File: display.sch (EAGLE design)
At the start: 69 parts, among them IC1 74595, IC2 74595, IC3 74595, IC4 74595

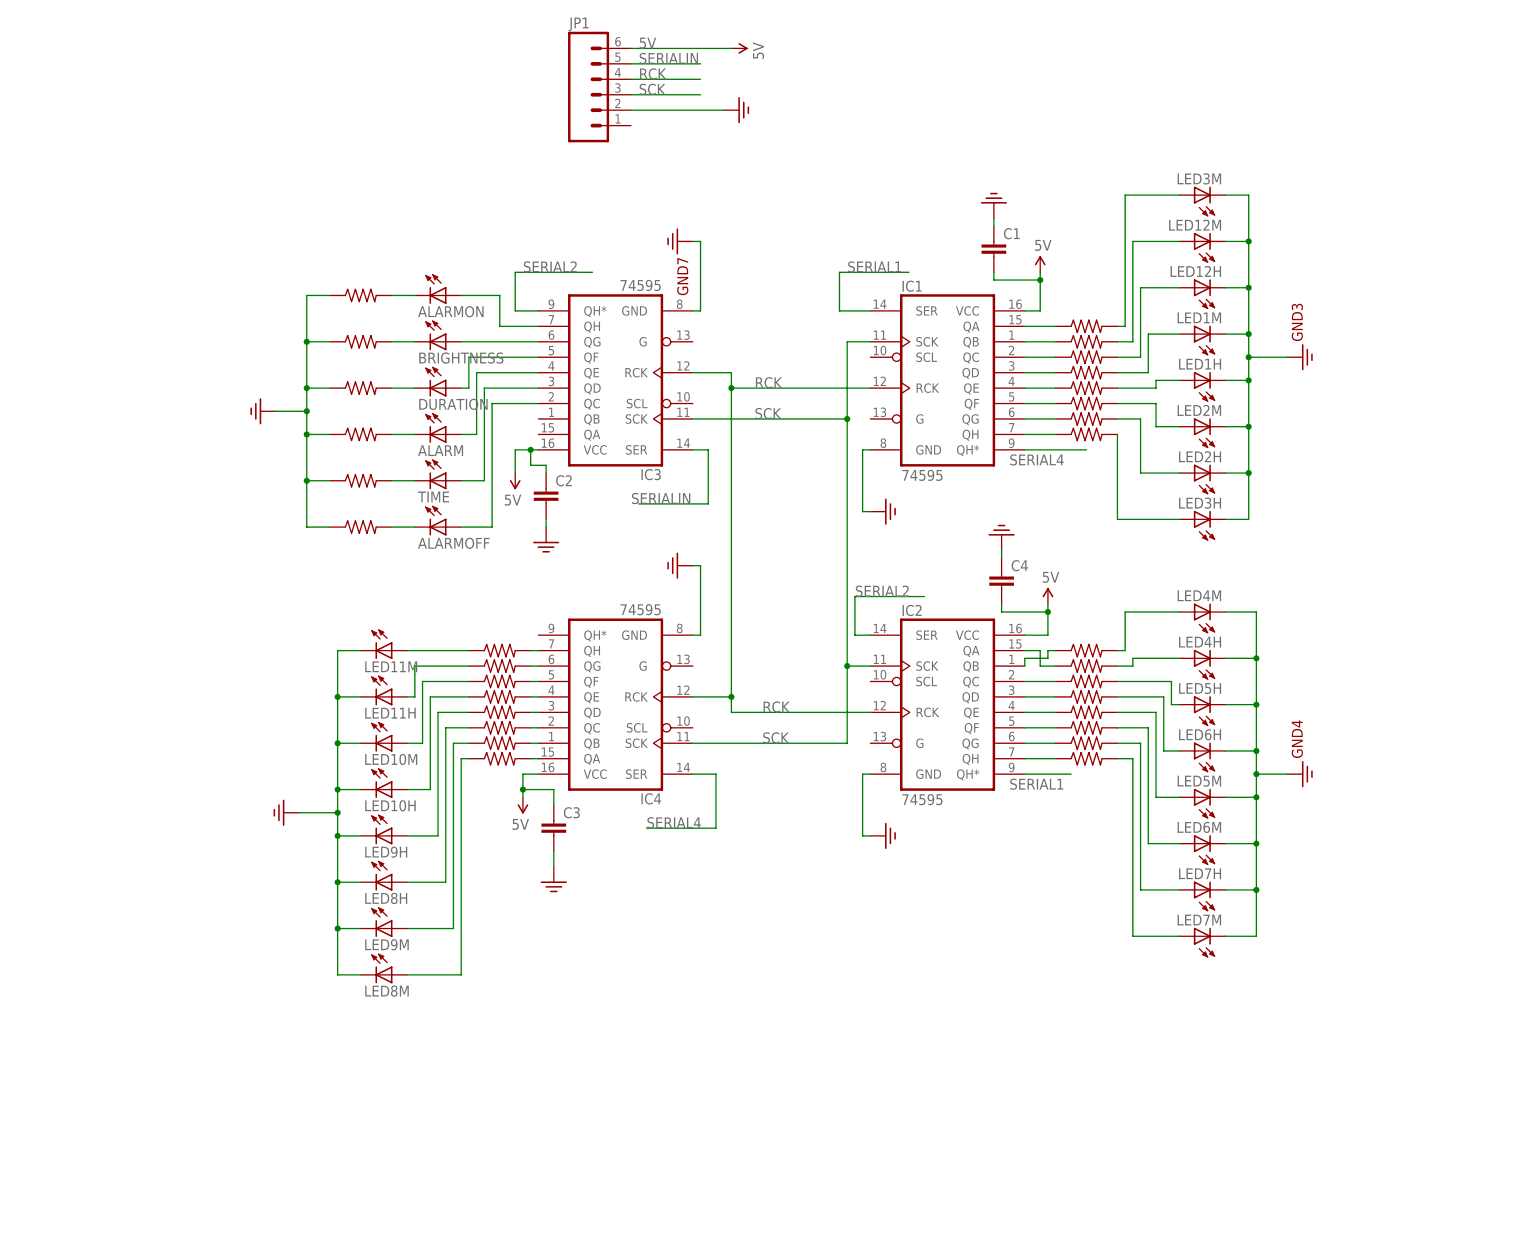
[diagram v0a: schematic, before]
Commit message: Renamed controller > display. Removed resitor names. Added IC1 QH to IC2 serial.
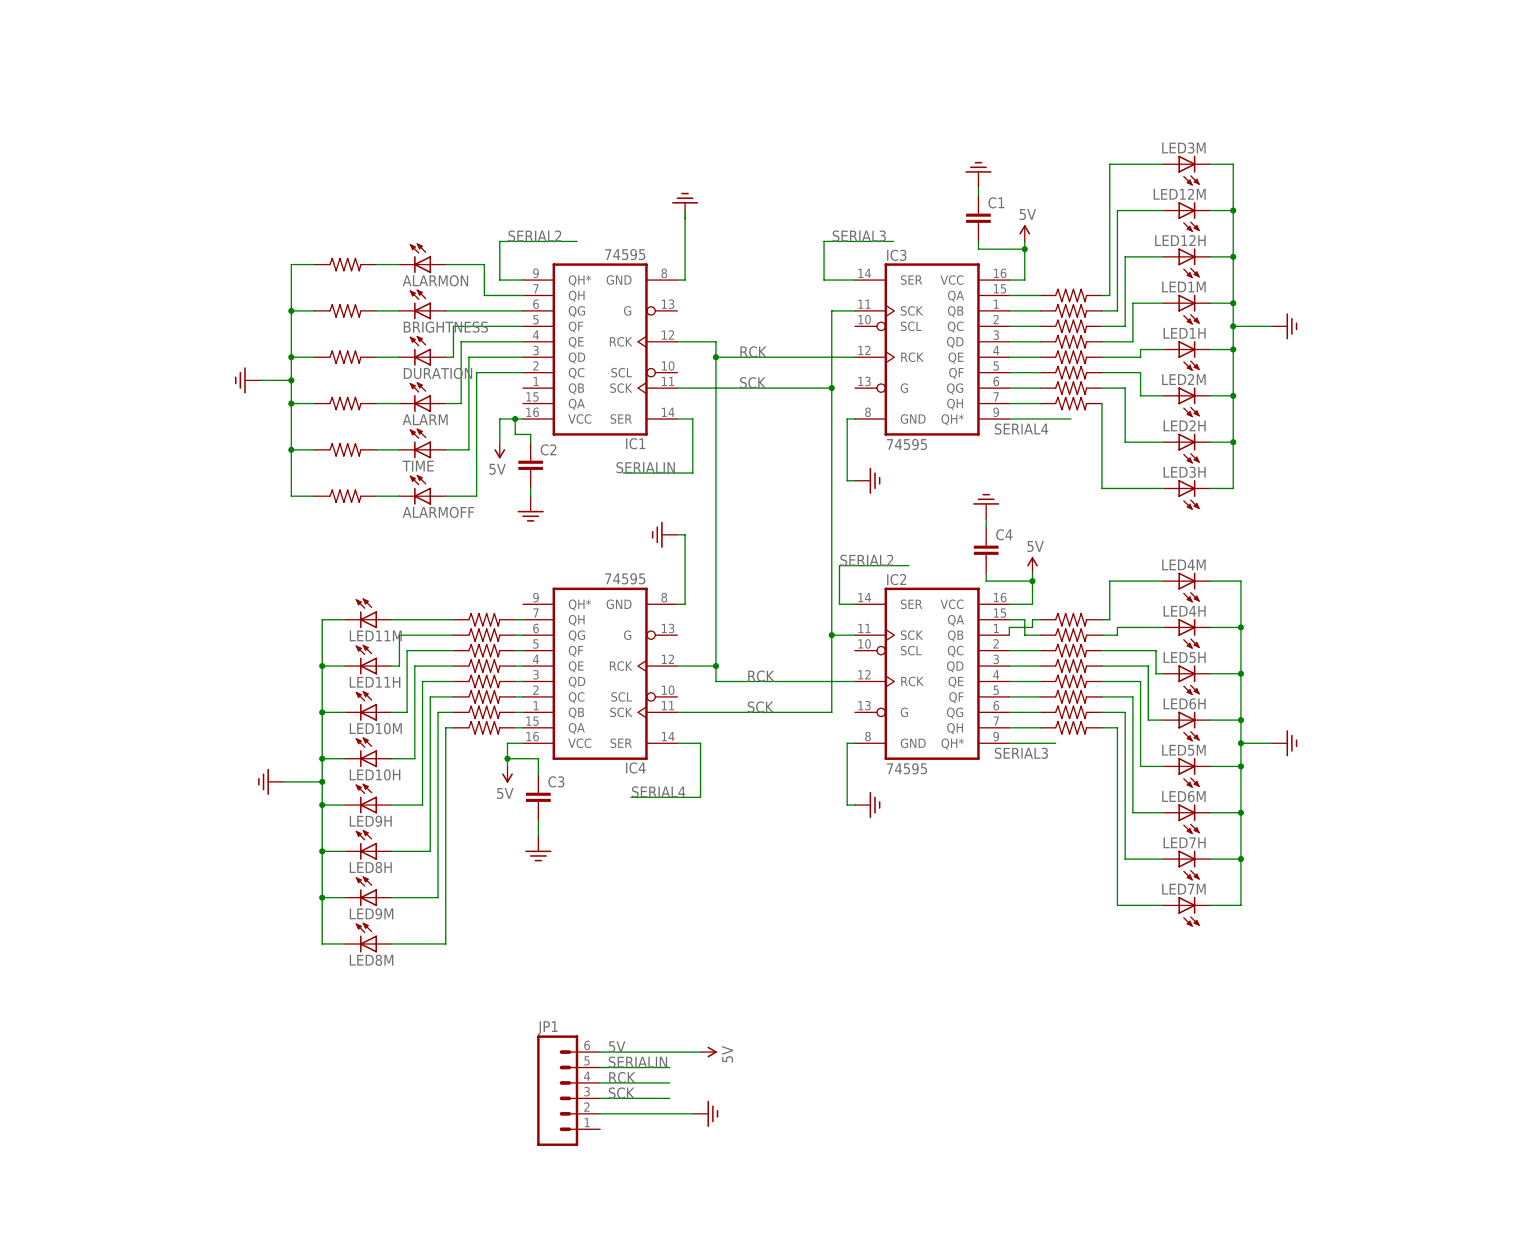
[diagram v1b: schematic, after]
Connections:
- removed net SERIAL1: IC1.SER, IC2.QH*
- new net SERIAL3: IC2.QH*, IC3.SER
- net N$14: now also IC3.QA; no longer IC1.QA
- net N$31: now also IC3.QB; no longer IC1.QB
- net N$32: now also IC3.QC; no longer IC1.QC
- net N$33: now also IC3.QD; no longer IC1.QD
- net N$34: now also IC3.QE; no longer IC1.QE
- net N$35: now also IC3.QF; no longer IC1.QF
- net N$36: now also IC3.QG; no longer IC1.QG
- net N$37: now also IC3.QH; no longer IC1.QH
- net N$49: now also IC1.QH; no longer IC3.QH
- net N$50: now also IC1.QG; no longer IC3.QG
- net N$52: now also IC1.QE; no longer IC3.QE
- net N$53: now also IC1.QD; no longer IC3.QD
- net N$54: now also IC1.QC; no longer IC3.QC
- net N$63: now also IC1.QF; no longer IC3.QF
- net SERIAL2: now also IC1.QH*; no longer IC3.QH*
- net SERIAL4: now also IC3.QH*; no longer IC1.QH*
- net SERIALIN: now also IC1.SER; no longer IC3.SER
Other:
- moved on the sheet: ALARM, ALARMOFF, ALARMON, BRIGHTNESS, C1, C2, C3, C4, DURATION, IC1, IC2, IC3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

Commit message: Beginning of new controller board layout.
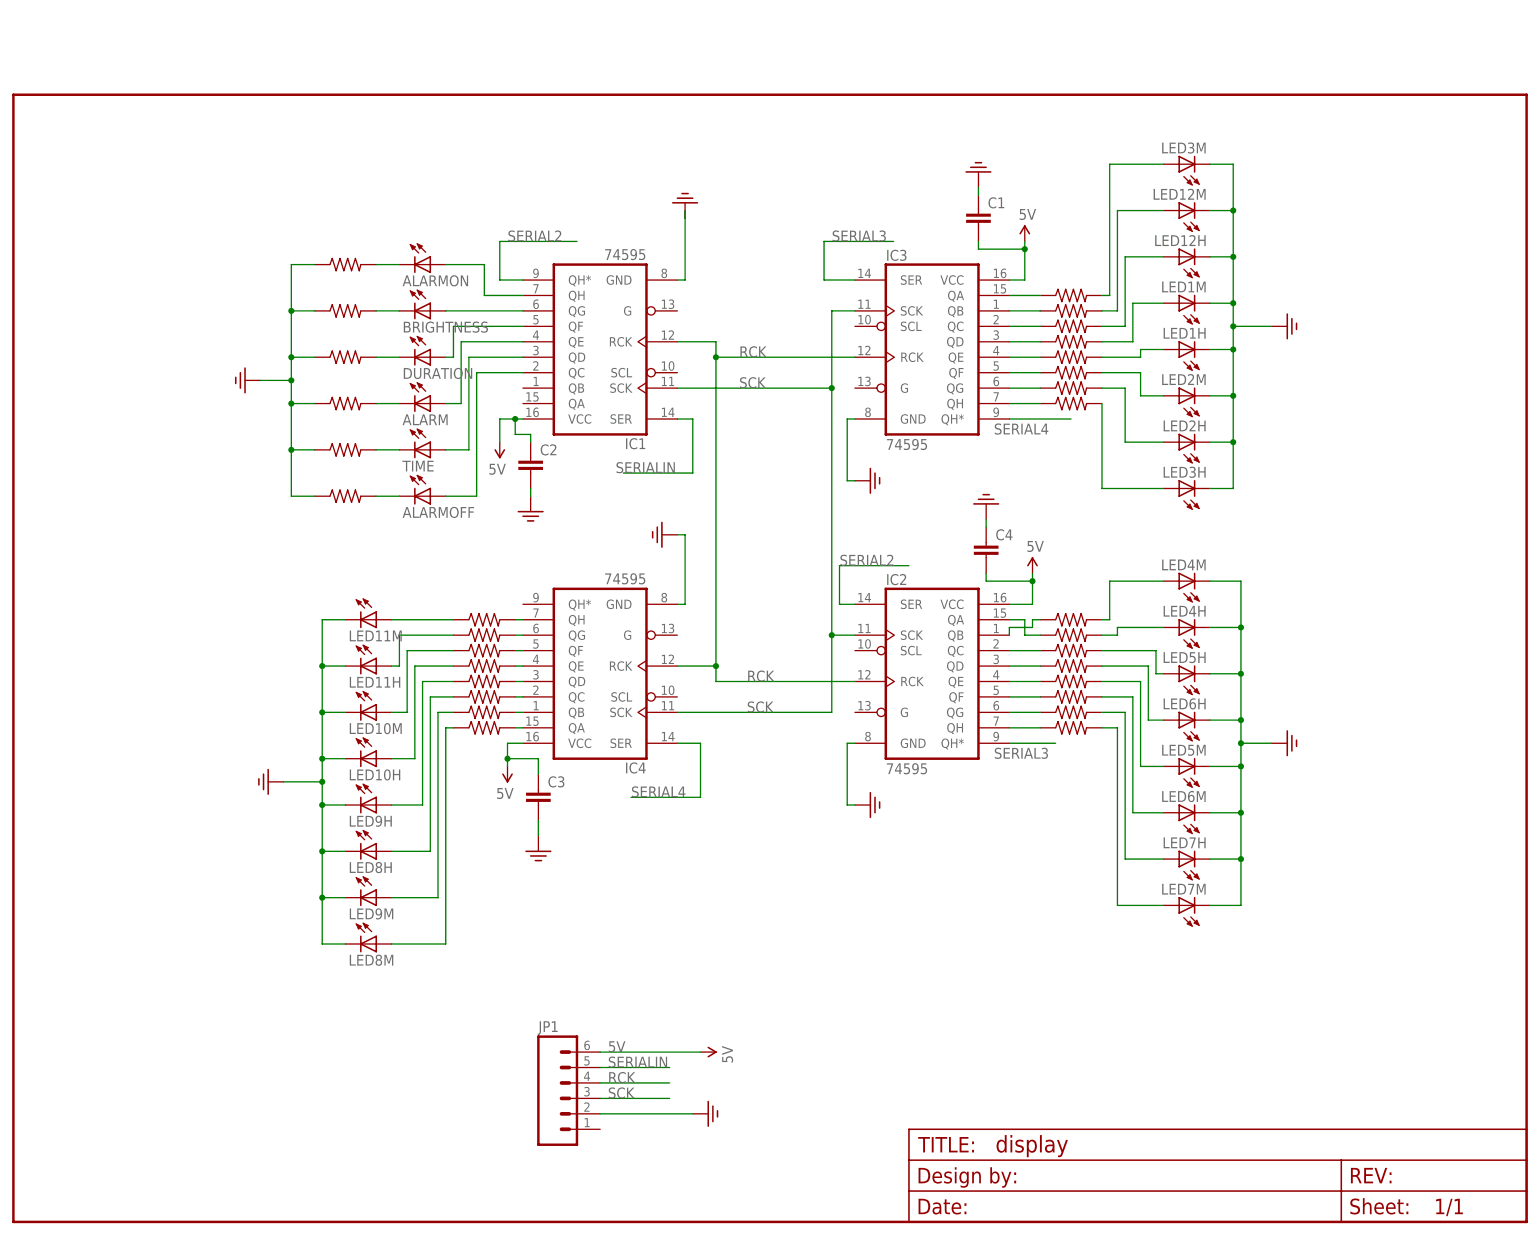
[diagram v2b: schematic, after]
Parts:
- added FRAME1: FRAME-LETTER, SparkFun-Aesthetics:FRAME-LETTER
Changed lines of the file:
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@@
 <part name="GND12" library="SparkFun-Aesthetics" deviceset="GND2" device=""/>
 <part name="GND13" library="SparkFun-Aesthetics" deviceset="GND2" device=""/>
+<part name="FRAME1" library="SparkFun-Aesthetics" deviceset="FRAME-LETTER" device=""/>
 </parts>
 <sheets>
@@
 <instance part="GND12" gate="G$1" x="86.36" y="60.96" smashed="yes"/>
 <instance part="GND13" gate="G$1" x="160.02" y="118.11" smashed="yes" rot="R180"/>
+<instance part="FRAME1" gate="G$1" x="0" y="0"/>
+<instance part="FRAME1" gate="G$2" x="147.32" y="0"/>
 </instances>
 <busses>
